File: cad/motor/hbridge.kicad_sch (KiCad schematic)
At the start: 21 parts, among them Q1 NMOS, Q15 NMOS, Q17 PMOS, Q19 PMOS, Q2 NMOS, Q21 PMOS, Q3 PMOS, Q4 PMOS, Q5 NMOS, Q7 PMOS, Q8 PMOS

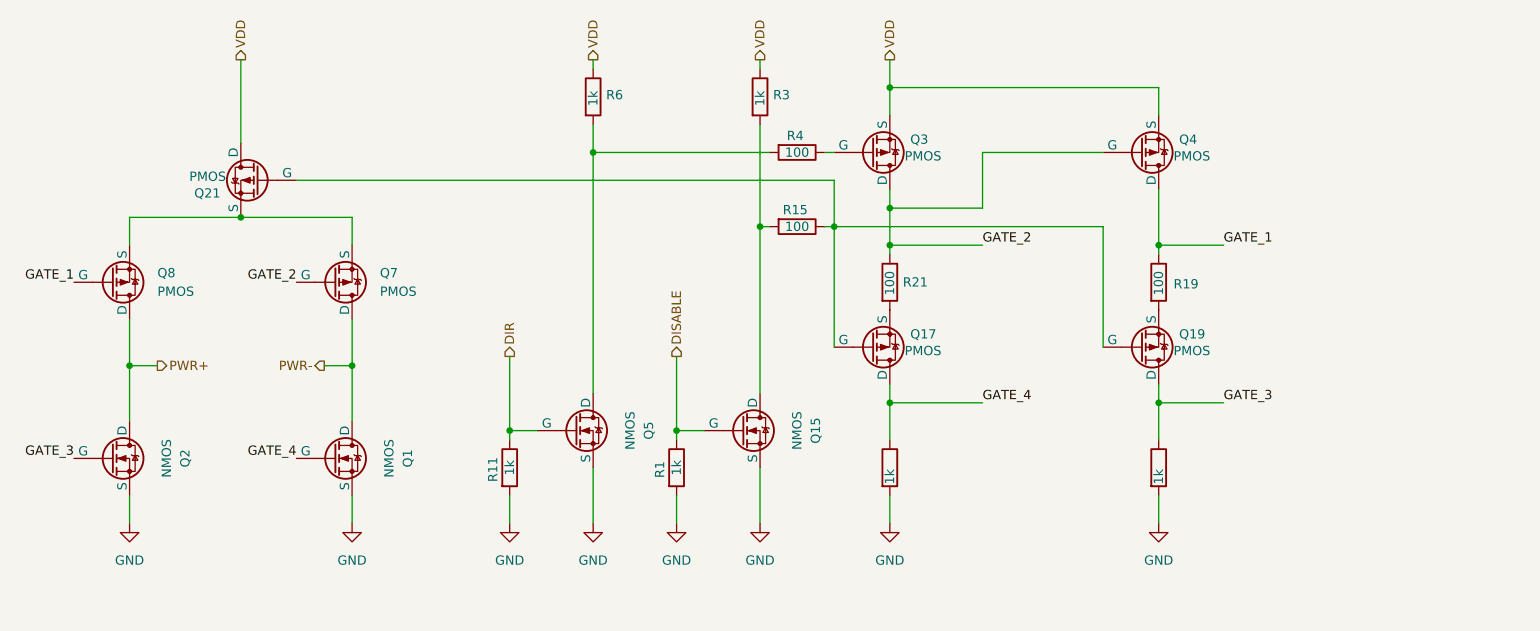
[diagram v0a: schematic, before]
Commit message: reliable enable/disable with capacitor
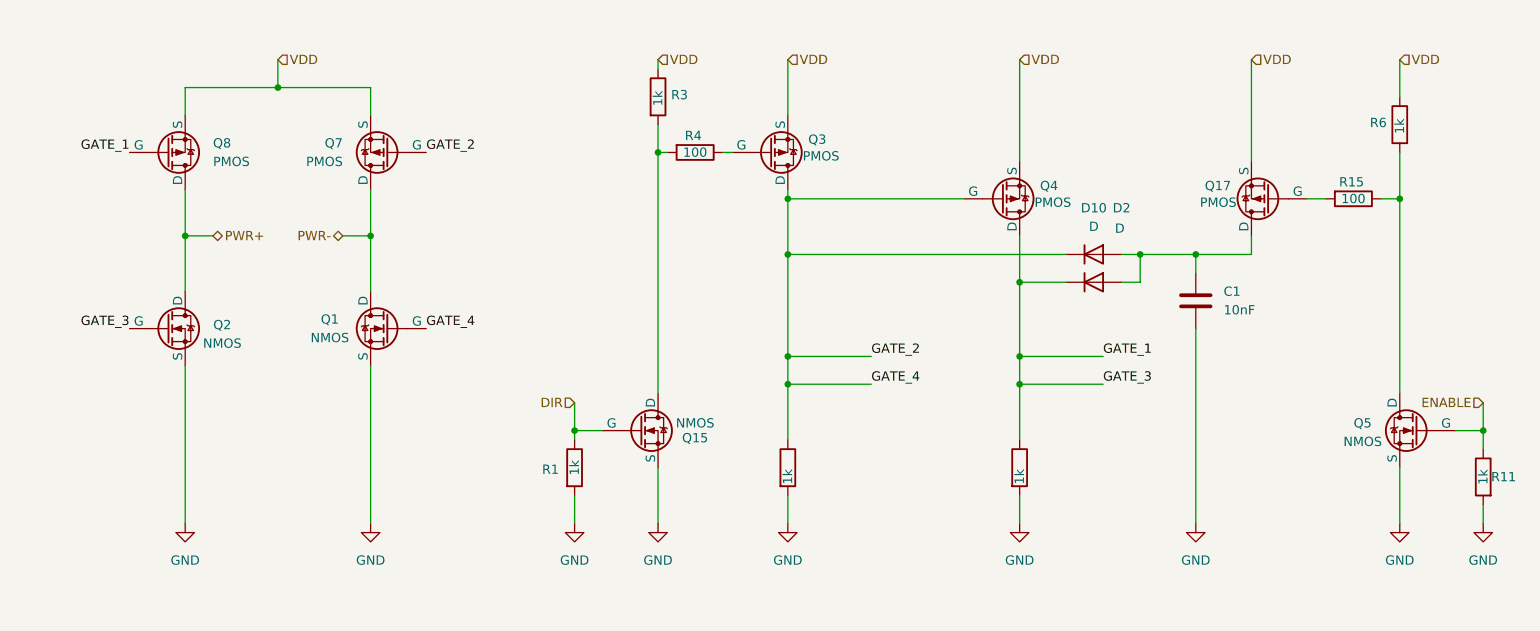
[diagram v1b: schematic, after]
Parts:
- removed Q19, Q21: PMOS, symbol Simulation_SPICE:PMOS
- removed R19, R21: 100, symbol Device:R
- added C1: 10nF, symbol Device:C
- added D10, D2: D, symbol Device:D
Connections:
- net DISABLE is gone; now on net DIR: Q15.2 (G), R1.1
- net GATE_3 is gone; now on net GATE_1: Q2.2 (G), R5.1
- net DIR: no longer Q5.2 (G), R11.1
- net GATE_1: now also D2.1 (K)
- net GATE_2: now also Q1.2 (G), R2.1, D10.1 (K)
- net GND: now also C1.2
- net VDD: now also Q17.3 (S), Q7.3 (S), Q8.3 (S)
- net at Q5.1 (D), R6.2: now also R15.1; no longer R4.2
- net at Q15.1 (D), R3.2: now also R4.2; no longer R15.2
- net at Q17.2 (G): now also R15.2; no longer R15.1
- removed net GATE_4: Q1.2 (G), Q17.1 (D), R2.1
- new net: C1.1, D10.2 (A), D2.2 (A), Q17.1 (D)
- new net ENABLE: Q5.2 (G), R11.1
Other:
- moved on the sheet: Q1, Q15, Q2, Q3, Q4, Q5, Q7, Q8, R1, R11, R3, R4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

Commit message: solve amp spikes
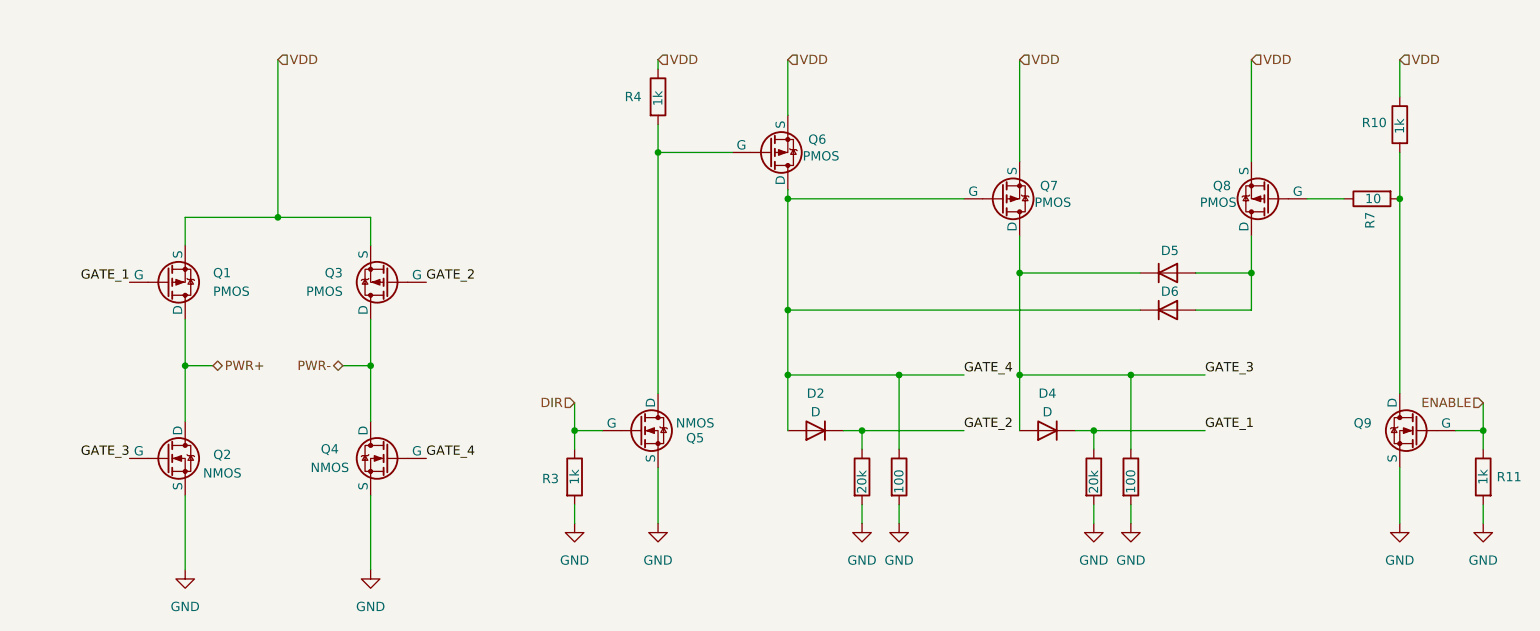
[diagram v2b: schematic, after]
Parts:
- removed C1: 10nF, symbol Device:C
- removed D10: D, symbol Device:D
- removed R15, R4: 100, symbol Device:R
- removed R2: 1k, symbol Device:R
- added D4, D5, D6: D, symbol Device:D
- added R6, R9: 100, symbol Device:R
- added R7: 10, symbol Device:R
- added R8: 20k, symbol Device:R
- R5: value 1k -> 20k
- renumbered Q8 to Q1, Q7 to Q3, Q1 to Q4, Q15 to Q5, Q3 to Q6, Q4 to Q7, Q17 to Q8, Q5 to Q9, R6 to R10, R1 to R3, R3 to R4
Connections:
- net GATE_1: now also D4.1 (K), R8.1; no longer D2.1 (K), Q2.2 (G), Q7.1 (D), R5.1
- net GATE_2: now also D2.1 (K), R5.1; no longer Q4.2 (G), Q6.1 (D), Q7.2 (G)
- net GND: now also R6.2, R8.2, R9.2
- net at Q8.1 (D): now also D5.2 (A), D6.2 (A); no longer D2.2 (A)
- net at Q6.2 (G): now also Q5.1 (D), R4.2
- net at Q8.2 (G): now also R7.1
- net at Q9.1 (D), R10.2: now also R7.2
- new net GATE_3: D4.2 (A), D5.1 (K), Q2.2 (G), Q7.1 (D), R9.1
- new net GATE_4: D2.2 (A), D6.1 (K), Q4.2 (G), Q6.1 (D), Q7.2 (G), R6.1
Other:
- moved on the sheet: Q1, Q2, Q3, Q4, R3
